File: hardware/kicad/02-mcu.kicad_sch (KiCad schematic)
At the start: 10 parts, among them SW14 BOOT, SW15 RESET, U1 ESP32-S3-N16R8

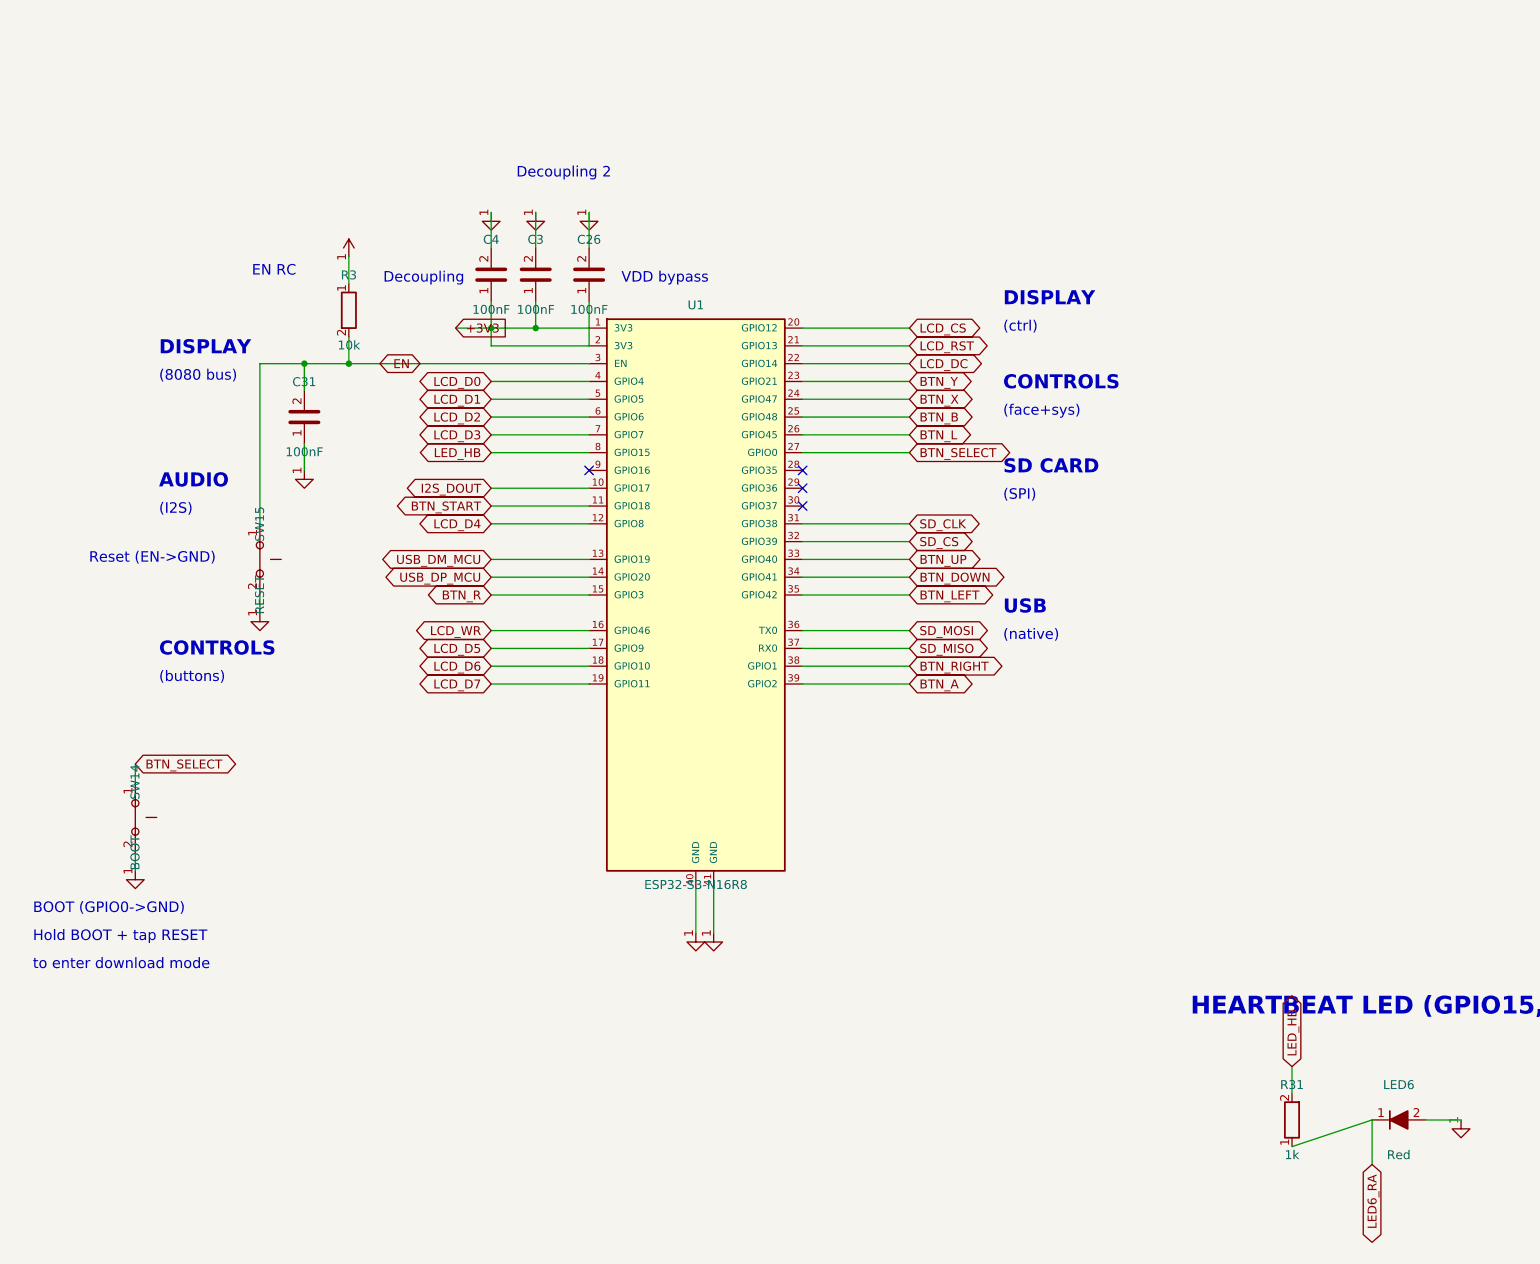
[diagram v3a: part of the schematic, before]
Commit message: schematic: zero rendered text overlaps + real P-MOSFET artwork for Q1/Q2
The rendered sheets carried 75 text-on-text collisions the overlap gate
could not see: its model missed pin-number digits, KiCad's mirrored
field justification on 180-degree symbols, and global-label extents.
Root fixes in the generator:

- symbol() now places Reference/Value per part class: beside the body
  for two-pin verticals (R/C/L/Battery), stacked above for LEDs and the
  big ICs whose bottom pin numbers the old centred Value printed over,
  with per-call overrides where a zone is tight. On 180-rotated symbols
  the emitted justification is pre-mirrored, because KiCad flips it.
- Q1/Q2 get PMOS_SOT23 — same pin coordinates as the BAT54C symbol they
  were drawn with (wires and netlist untouched), but the artwork is now
  a P-MOSFET instead of a dual Schottky diode.
- Sheet-level relayouts: decoupling row on 02 spread to 11 mm pitch,
  menu-combo D1 zone on 06, FPC header on 03, PAM bias notes on 04,
  IP5306 KEY exit and the whole power-switch zone on 01.
- ESP32 module pin 41 name blanked — two "GND"s 2.54 mm apart printed
  into each other; number, type and net unchanged.

New gate: verify_schematic_render_overlaps.py exports each sheet to SVG
via kicad-cli and fails if any two DRAWN text runs intersect — ground
truth instead of a re-derived model (47 hits on the old sheet 01, 0
now). Wired into verify-all; dispatch mutation tests 14/14.

Netlist invariance: verify_netlist_diff 4/4, ERC clean at every
severity, schematic-PCB sync green. Website SVG/PDF re-rendered.

Co-Authored-By: Claude Fable 5 <noreply@anthropic.com>
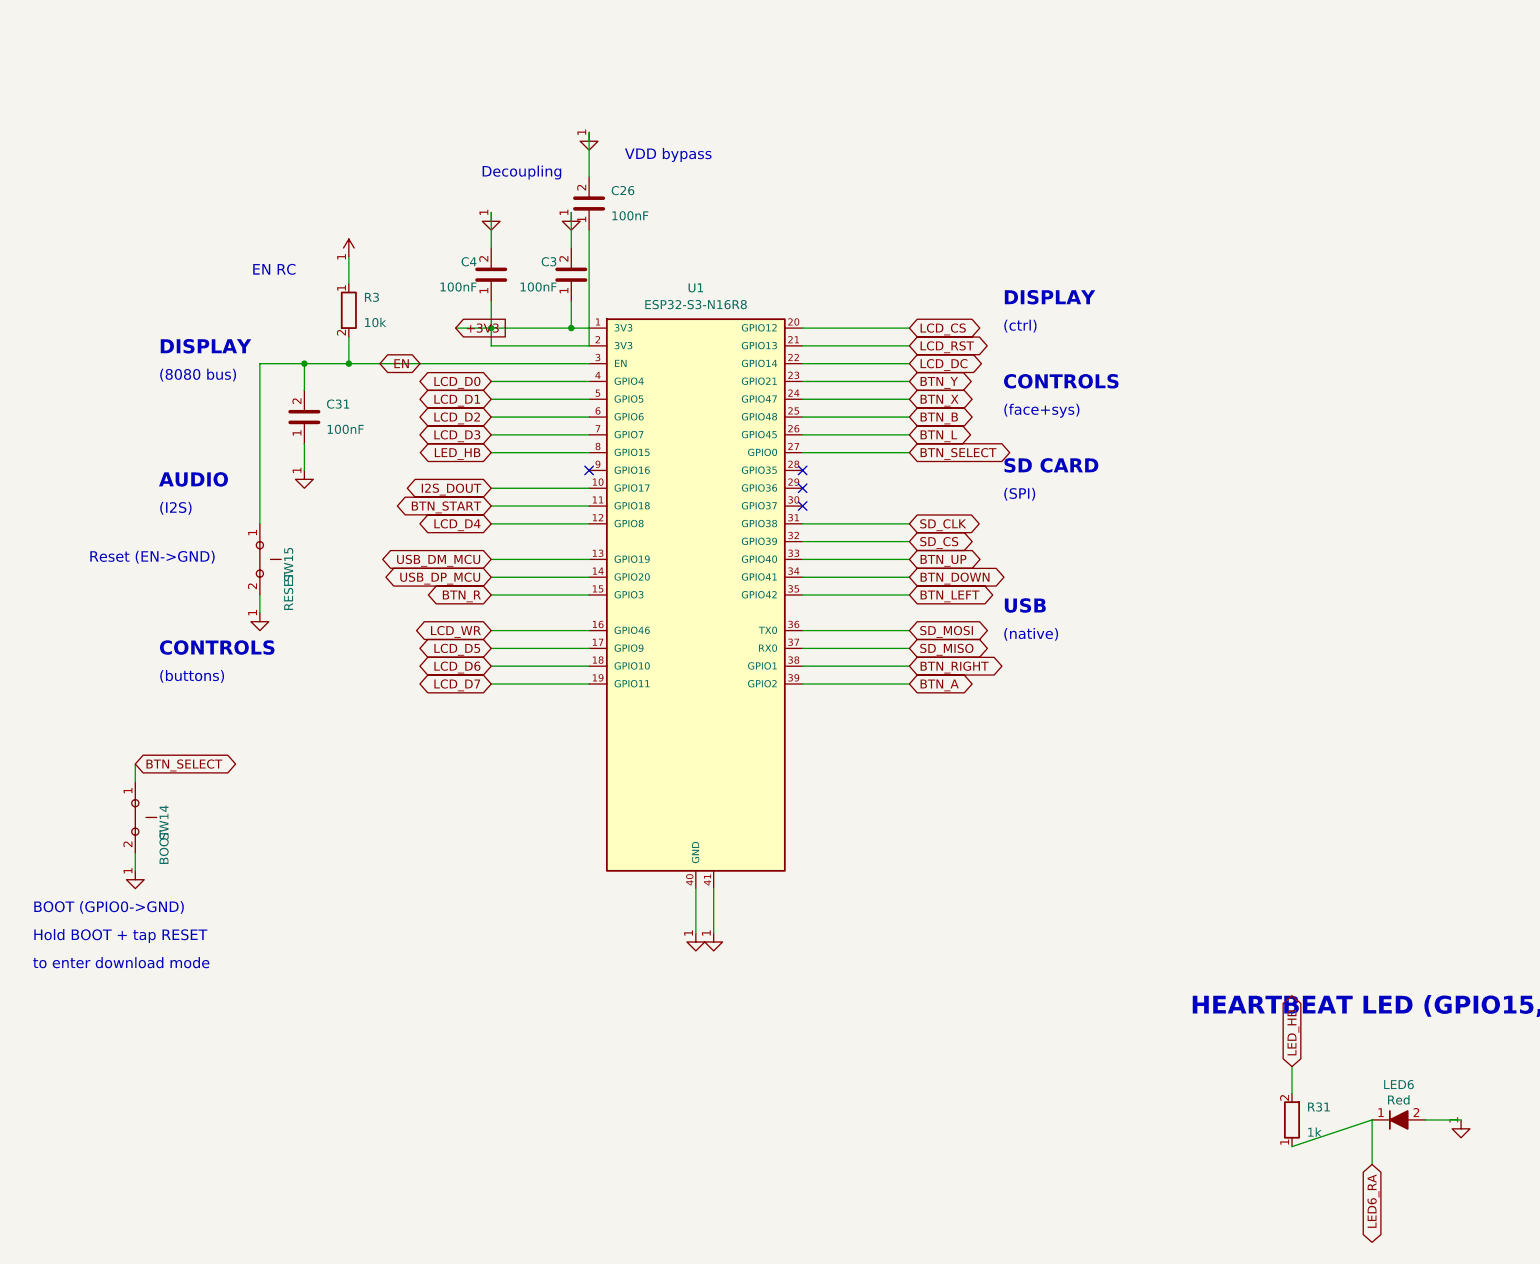
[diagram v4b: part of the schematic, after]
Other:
- note removed: "Decoupling 2"
- moved on the sheet: C26, C3

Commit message: audit R32: retire every stale backlight/EN/audio text the R31 round flagged
Round 32 (first audit of the merged SW16 respin, at c98287a): Layer 1
fully green, no new electrical findings. This commit closes the
stale-text batch:

- R32-LOW-1 + R31-MED-4: mcu.py GPIO ASSIGNMENT TABLE now prints the
  real backlight rail ("BL +5V via R27") and the real audio pinout
  ("PDM TX: GPIO17=DOUT GPIO15=LED_HB GPIO16 free") instead of the
  retired BCLK/LRCK story. 02-mcu.kicad_sch regenerated.
- R31-LOW-6: board_config.h + display.c backlight comments (5 sites)
  reworded from "tied to 3V3" to load-side +5V via R27 (net LED_BLA).
- R31-LOW-11: hardware-audit skill no longer teaches false baselines —
  domain-checks.md EN bullet rewritten to the R3 10k + C31 100nF truth,
  backlight bullet to the R27/LED_BLA fix; SKILL.md "must NOT re-raise"
  list trimmed to the genuinely settled decisions and the stale macOS
  cd path corrected.
- hardware-audit-bugs.md: Round 32 report appended with fix statuses.

verify_dfa 10/10; make verify-all 103/103 (incl. the render-overlap
gate on the regenerated MCU sheet).

Co-Authored-By: Claude Fable 5 <noreply@anthropic.com>
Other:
- note added: "Audio (PDM TX):"
- note added: "GPIO17=DOUT GPIO15=LED_HB GPIO16 free"
- note added: "GPIO46=WR (RD tied +3V3; BL +5V via R27)"
- note removed: "Audio (I2S):"
- note removed: "GPIO15=BCLK GPIO16=LRCK GPIO17=DOUT"
- note removed: "GPIO46=WR (RD/BL tied +3V3 on FPC)"
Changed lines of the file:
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@@
   (text "GPIO4-11 = D0-D7 (8-bit data bus)" (at 320 45 0) (effects (font (size 2.54 2.54)) (justify left)))
   (text "GPIO12=CS  GPIO13=RST  GPIO14=DC" (at 320 50 0) (effects (font (size 2.54 2.54)) (justify left)))
-  (text "GPIO46=WR  (RD/BL tied +3V3 on FPC)" (at 320 55 0) (effects (font (size 2.54 2.54)) (justify left)))
-  (text "Audio (I2S):" (at 320 63 0) (effects (font (size 2 2) bold) (justify left)))
-  (text "GPIO15=BCLK  GPIO16=LRCK  GPIO17=DOUT" (at 320 68 0) (effects (font (size 2.54 2.54)) (justify left)))
+  (text "GPIO46=WR  (RD tied +3V3; BL +5V via R27)" (at 320 55 0) (effects (font (size 2.54 2.54)) (justify left)))
+  (text "Audio (PDM TX):" (at 320 63 0) (effects (font (size 2 2) bold) (justify left)))
+  (text "GPIO17=DOUT  GPIO15=LED_HB  GPIO16 free" (at 320 68 0) (effects (font (size 2.54 2.54)) (justify left)))
   (text "SD Card (SPI):" (at 320 76 0) (effects (font (size 2 2) bold) (justify left)))
   (text "GPIO44=MOSI  GPIO43=MISO  GPIO38=CLK  GPIO39=CS" (at 320 81 0) (effects (font (size 2.54 2.54)) (justify left)))

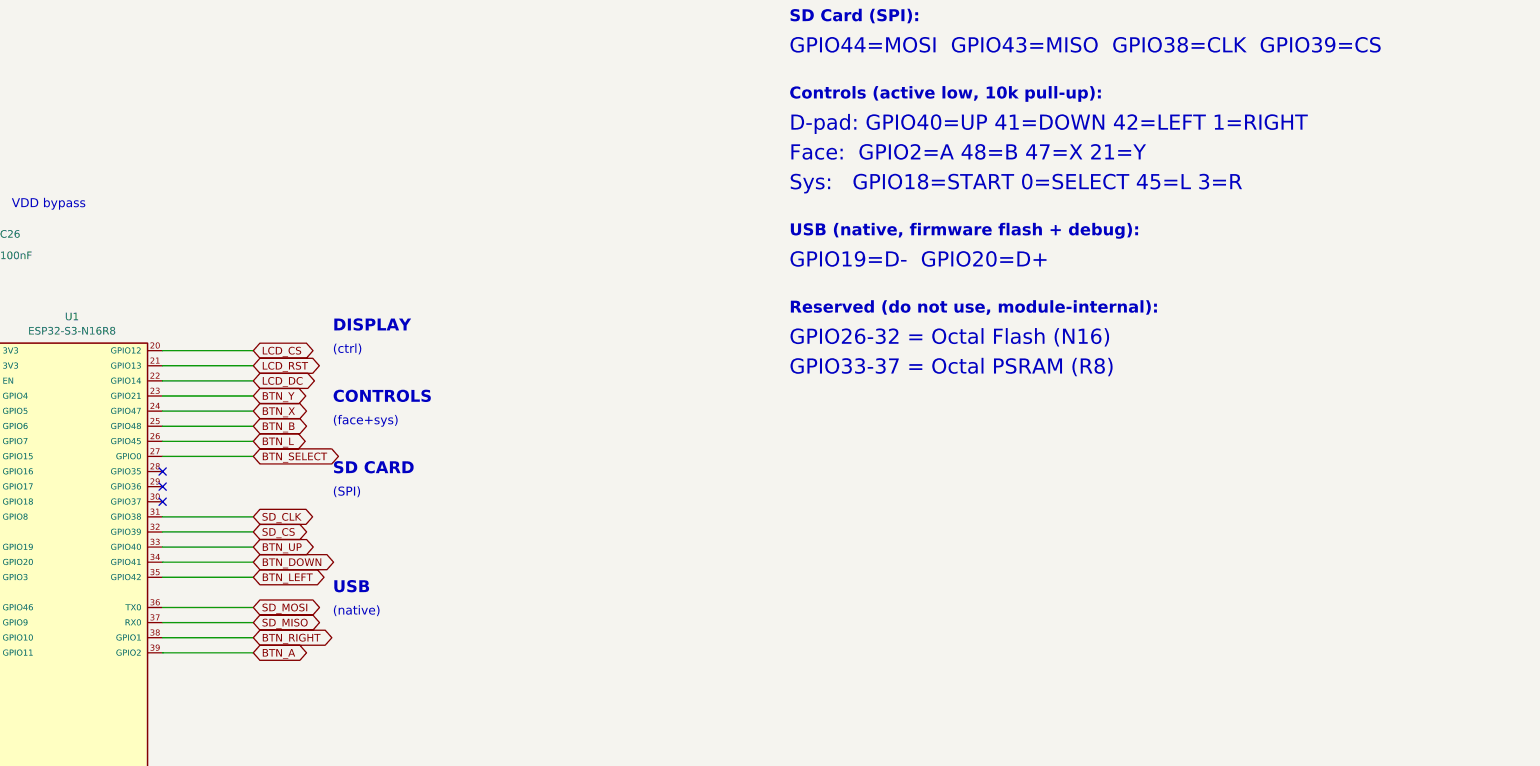
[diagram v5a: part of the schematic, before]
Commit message: Retro-Go first boot on the first article + R39-HIGH-1 (module pins 38/39 swapped)
Phase 2.8 reached: Retro-Go runs on article 0003 — launcher, SD, all 12
buttons, Owlia (NES) and Mario Bros played. Fork fixes are in the
submodule (0e533078, 53878dcb): i80 0x2C/0x3C continuation, landscape
480x320, PDM channel off at volume 0, RIGHT/A swap, L/R in the launcher.

R39-HIGH-1: the WROOM-1 datasheet has pin 38 = IO2 and pin 39 = IO1;
every project table (generator _PIN_TO_GPIO, datasheet_specs, schematic
pin table + symbol, board_config.h, Retro-Go target) had them swapped,
and verify_dfm_v2 asserted the wrong fact. Pins 4-37 re-verified against
the datasheet: only this pair. The copper is right — BTN_RIGHT is on pad
38 = GPIO2, BTN_A on pad 39 = GPIO1 — so the fix is names only:
BTN_RIGHT=GPIO2, BTN_A=GPIO1 everywhere; the regenerated PCB is
byte-identical to the built board; schematics, symbol, bring-up firmware,
net-explorer data and docs regenerated. Gate now asserts 38=GPIO2 and
39=GPIO1. verify-all green, verify_dfa 10/10, retro-go sync 63/63.

Also: prebuilt Retro-Go binaries refreshed, Phase 2 docs switched to
landscape scaling, .gitignore keeps every ROM under test-roms/ out of git
except the committed homebrew set, session log extended.

Co-Authored-By: Claude Opus 5 (1M context) <noreply@anthropic.com>
Claude-Session: https://claude.ai/code/session_01MsWyvkWxko6nCK1kvUkZjV
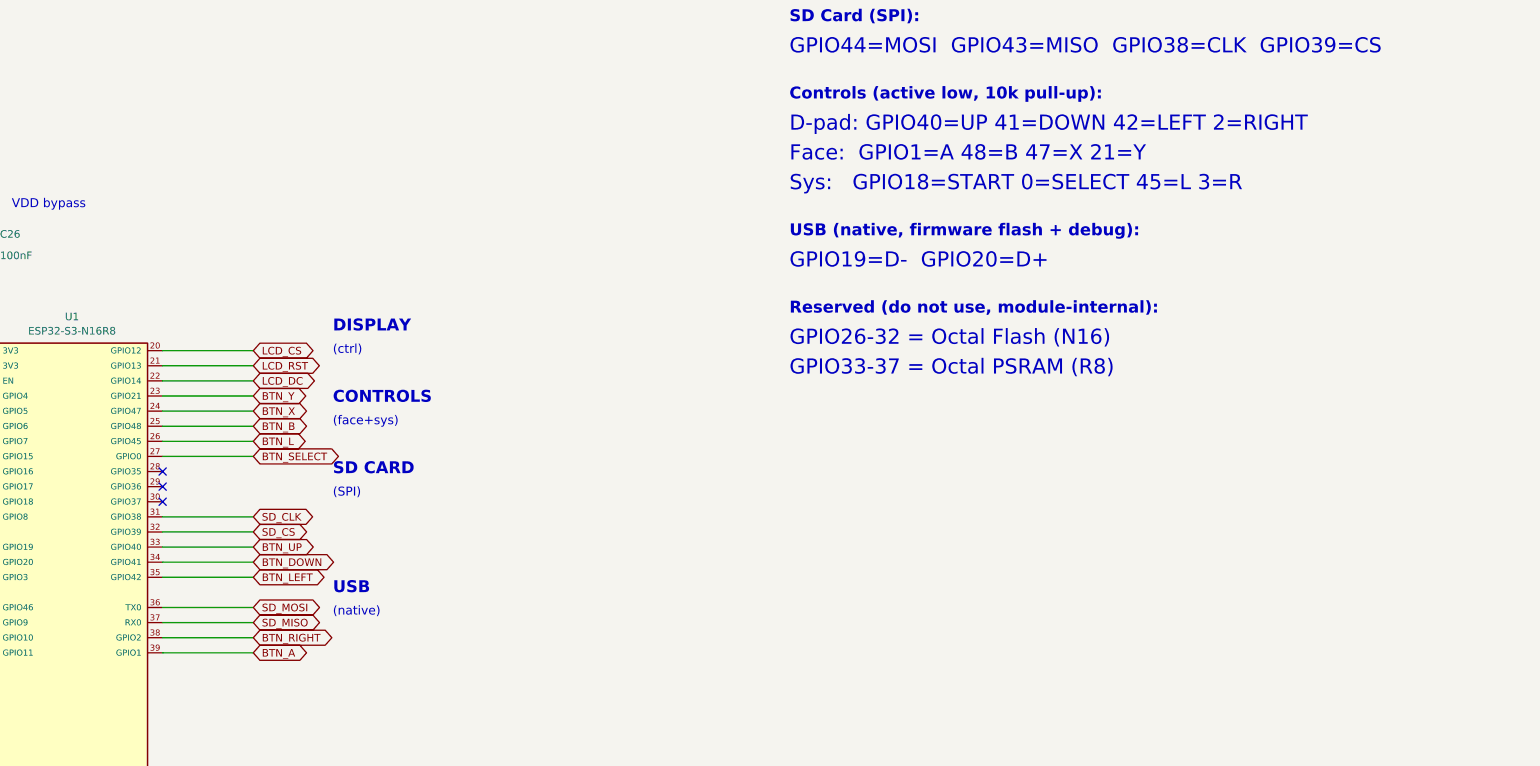
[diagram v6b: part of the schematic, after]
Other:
- note added: "D-pad: GPIO40=UP 41=DOWN 42=LEFT 2=RIGHT"
- note added: "Face: GPIO1=A 48=B 47=X 21=Y"
- note removed: "D-pad: GPIO40=UP 41=DOWN 42=LEFT 1=RIGHT"
- note removed: "Face: GPIO2=A 48=B 47=X 21=Y"
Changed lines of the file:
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@@
   (text "GPIO44=MOSI  GPIO43=MISO  GPIO38=CLK  GPIO39=CS" (at 320 81 0) (effects (font (size 2.54 2.54)) (justify left)))
   (text "Controls (active low, 10k pull-up):" (at 320 89 0) (effects (font (size 2 2) bold) (justify left)))
-  (text "D-pad: GPIO40=UP 41=DOWN 42=LEFT 1=RIGHT" (at 320 94 0) (effects (font (size 2.54 2.54)) (justify left)))
-  (text "Face:  GPIO2=A 48=B 47=X 21=Y" (at 320 99 0) (effects (font (size 2.54 2.54)) (justify left)))
+  (text "D-pad: GPIO40=UP 41=DOWN 42=LEFT 2=RIGHT" (at 320 94 0) (effects (font (size 2.54 2.54)) (justify left)))
+  (text "Face:  GPIO1=A 48=B 47=X 21=Y" (at 320 99 0) (effects (font (size 2.54 2.54)) (justify left)))
   (text "Sys:   GPIO18=START 0=SELECT 45=L 3=R" (at 320 104 0) (effects (font (size 2.54 2.54)) (justify left)))
   (text "USB (native, firmware flash + debug):" (at 320 112 0) (effects (font (size 2 2) bold) (justify left)))
